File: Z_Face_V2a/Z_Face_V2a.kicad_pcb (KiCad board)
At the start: 4 copper layers, 100 x 100 mm, 27 parts, among them J1 FC Connection, J4 Conn_01x01, J5 Conn_01x01, J6 Conn_01x01, J7 Conn_01x01, U1 VEML7700, U2 DRV2605LDGS, U3 MCP9808T-E/MS

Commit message: Blow up the layout
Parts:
- added C4: 100nF, Capacitor_SMD:C_0402_1005Metric, F.Cu at (219.3, 86.5)
- added C5: 10nF, Capacitor_SMD:C_0805_2012Metric, F.Cu at (219.3, 89.5)
- added C6: 100nF, Capacitor_SMD:C_0402_1005Metric, F.Cu at (138.0, 96.8)
- added J2: DF11 FC Connection, Connector_Hirose:Hirose_DF11-6DP-2DSA_2x03_P2.00mm_Vertical, B.Cu at (216.8, 109.1)
- added R2: 10k, Resistor_SMD:R_0603_1608Metric, F.Cu at (215.1, 81.6)
- added R3: 10k, Resistor_SMD:R_0603_1608Metric, F.Cu at (215.1, 84.1)
- added R4: 10k, Resistor_SMD:R_0603_1608Metric, F.Cu at (215.1, 86.6)
- added R5: 10k, Resistor_SMD:R_0603_1608Metric, F.Cu at (215.1, 89.1)
- added U4: TCA4311A, Package_SO:VSSOP-8_3x3mm_P0.65mm, F.Cu at (220.8, 82.7)
- C1: value 1uF -> 100nF; footprint Capacitor_SMD:C_0805_2012Metric -> Capacitor_SMD:C_0402_1005Metric
- J1: value FC Connection -> Molex FC Connection
- R1: value 1k -> 10k
- U3: value MCP9808T-E/MS -> MCP9808_DFN
- moved U1 28.8 mm to (136.0, 98.5), turned to -135 degrees
- moved J1 12.6 mm to (140.5, 75.5)
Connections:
- J1 pad 2: SDA -> /SDAIN
- J1 pad 3: SCL -> /SCLIN
- J1 pad 5: GND -> VSOLAR
- U1 pad 1: SCL -> /SCL
- U1 pad 4: SDA -> /SDA
- U2 pad 2: SCL -> /SCL
- U2 pad 3: SDA -> /SDA
- U3 pad 1: SDA -> /SDA
- U3 pad 2: SCL -> /SCL
- U3 pad 3: (no net) -> unconnected-(U3-Alert-Pad3)
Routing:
- net SDA: track 45.3 -> 0.00 mm, vias 5 -> 0
- net SCL: track 35.7 -> 0.00 mm, vias 1 -> 0
- net /SDA: track 0.00 -> 23.4 mm, vias 0 -> 1
- net /SCL: track 0.00 -> 19.6 mm, vias 0 -> 2
- net GND: track 61.4 -> 52.9 mm, vias 52 -> 49
- net VSOLAR: track 184.2 -> 182.3 mm
- net +3V3: track 52.5 -> 51.9 mm

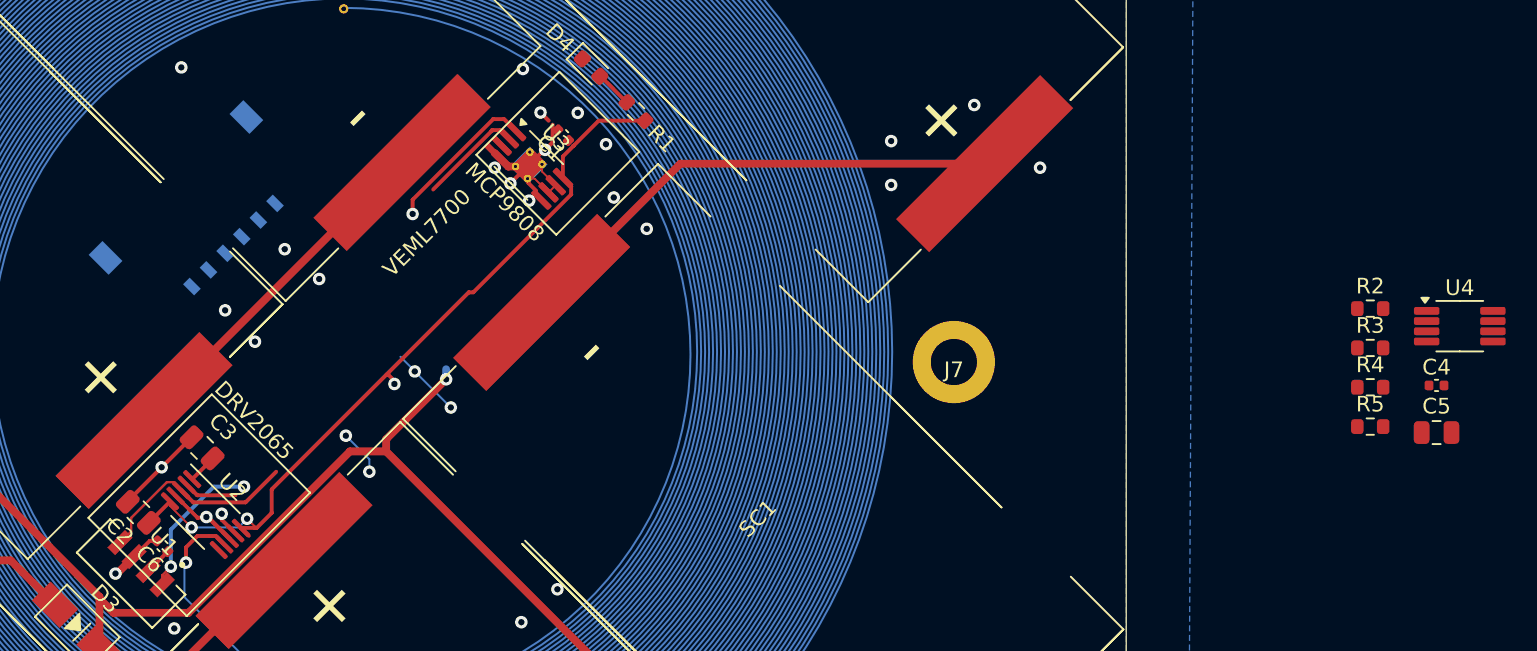
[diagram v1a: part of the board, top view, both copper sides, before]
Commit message: Z- V2a: Changed Passives to 0402
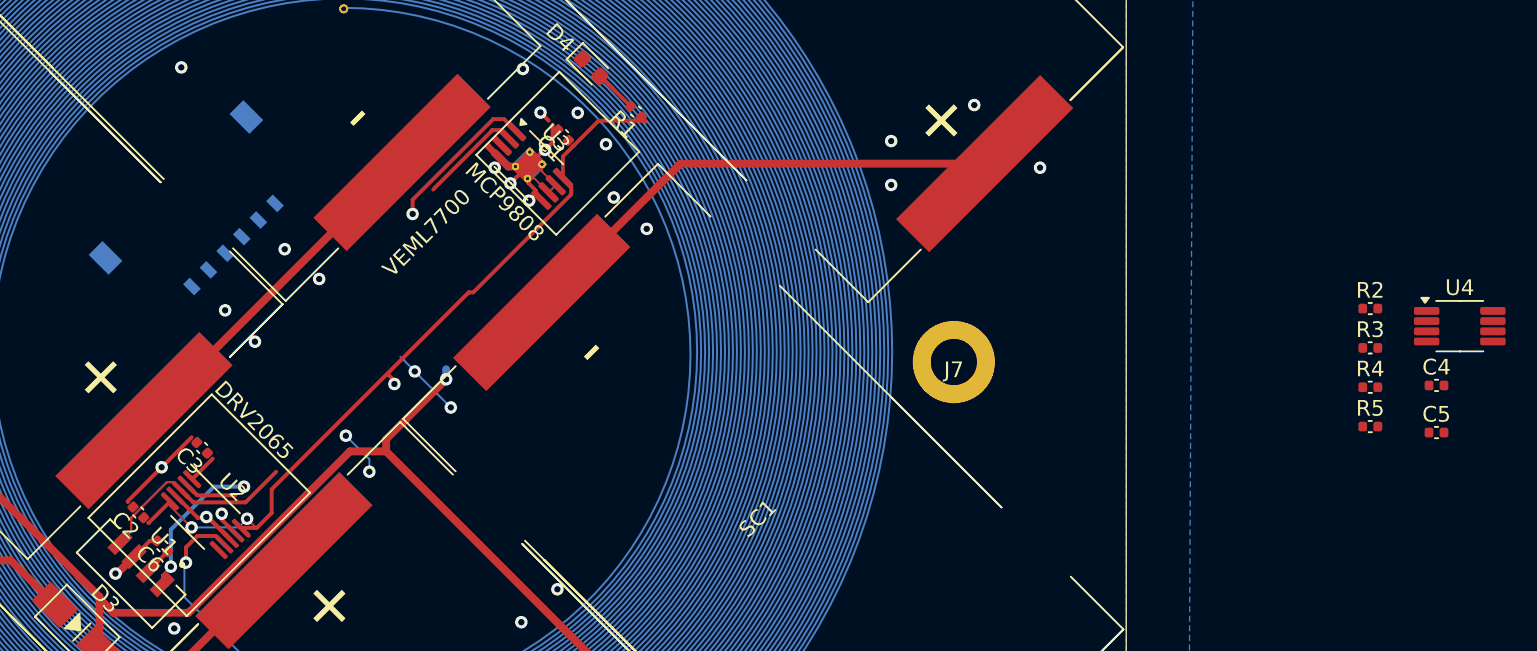
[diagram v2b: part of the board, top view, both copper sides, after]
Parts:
- C2, C3, C5: footprint Capacitor_SMD:C_0805_2012Metric -> Capacitor_SMD:C_0402_1005Metric
- R1, R2, R3, R4, R5: footprint Resistor_SMD:R_0603_1608Metric -> Capacitor_SMD:C_0402_1005Metric

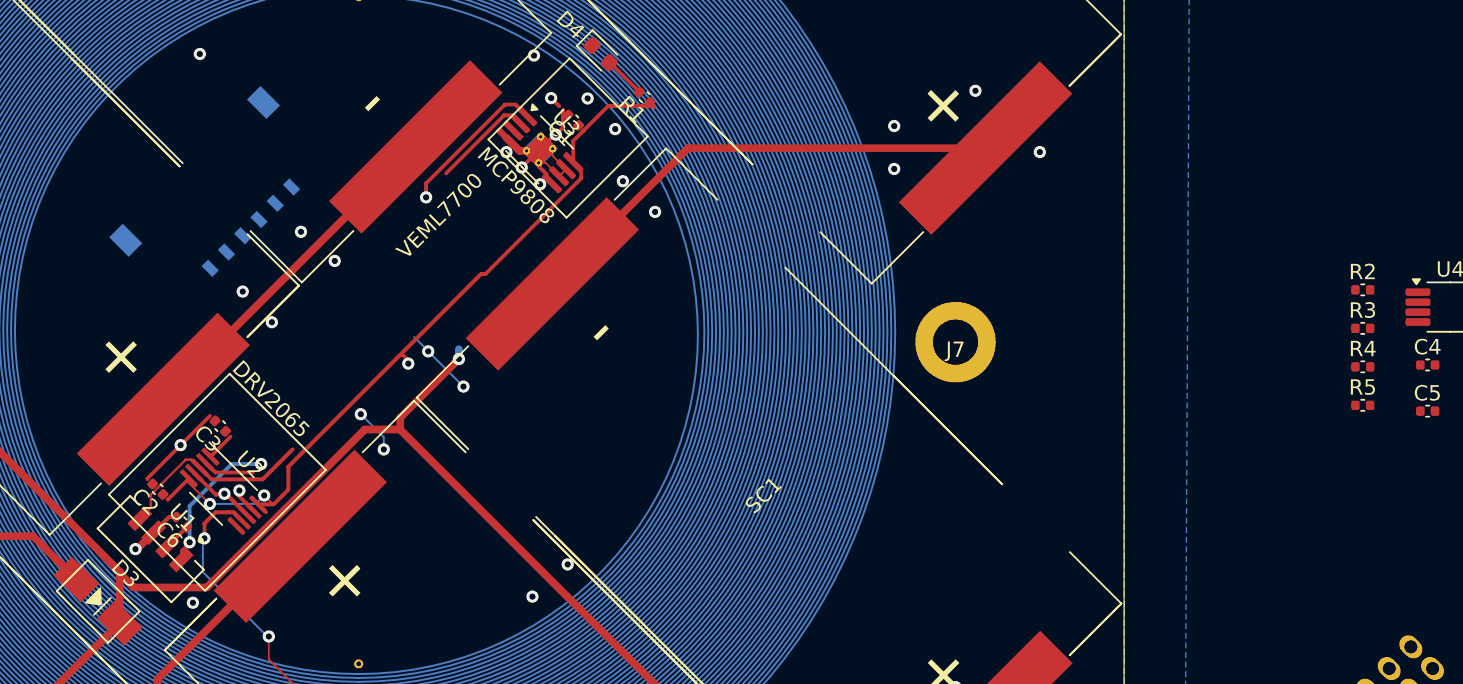
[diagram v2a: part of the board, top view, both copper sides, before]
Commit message: Z- V2a: Replaced MCP9808 with TMP112
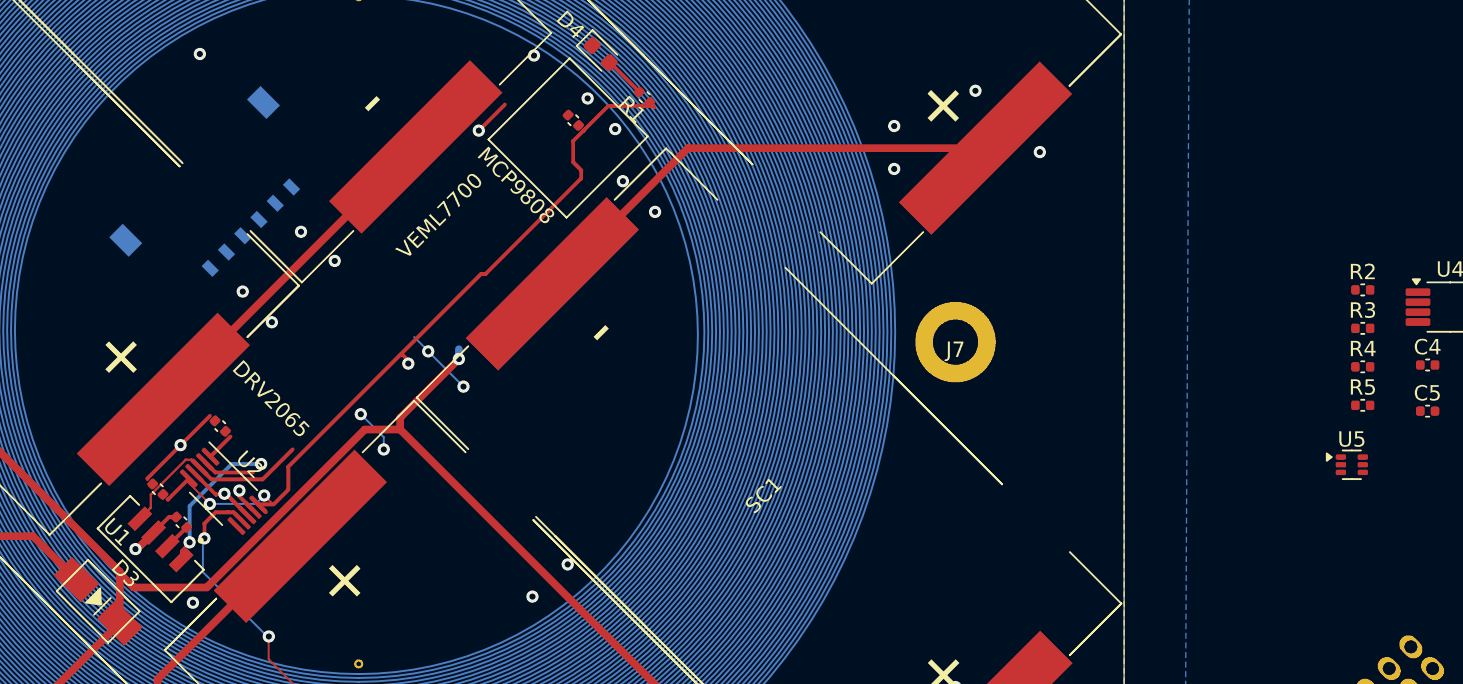
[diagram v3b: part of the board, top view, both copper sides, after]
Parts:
- removed U3: MCP9808_DFN, Package_SO:MSOP-8-1EP_3x3mm_P0.65mm_EP1.5x1.8mm_ThermalVias
- added U5: TMP112xxDRL, Package_TO_SOT_SMD:SOT-563, F.Cu at (214.4, 93.0)
- C1: value 100nF -> 10nF
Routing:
- net GND: track 52.9 -> 37.9 mm, vias 49 -> 44
- net /SDA: track 23.4 -> 15.8 mm
- net /SCL: track 19.6 -> 12.9 mm
